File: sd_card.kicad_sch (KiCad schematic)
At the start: 19 parts, among them J1101 DM3AT-SF-PEJM5

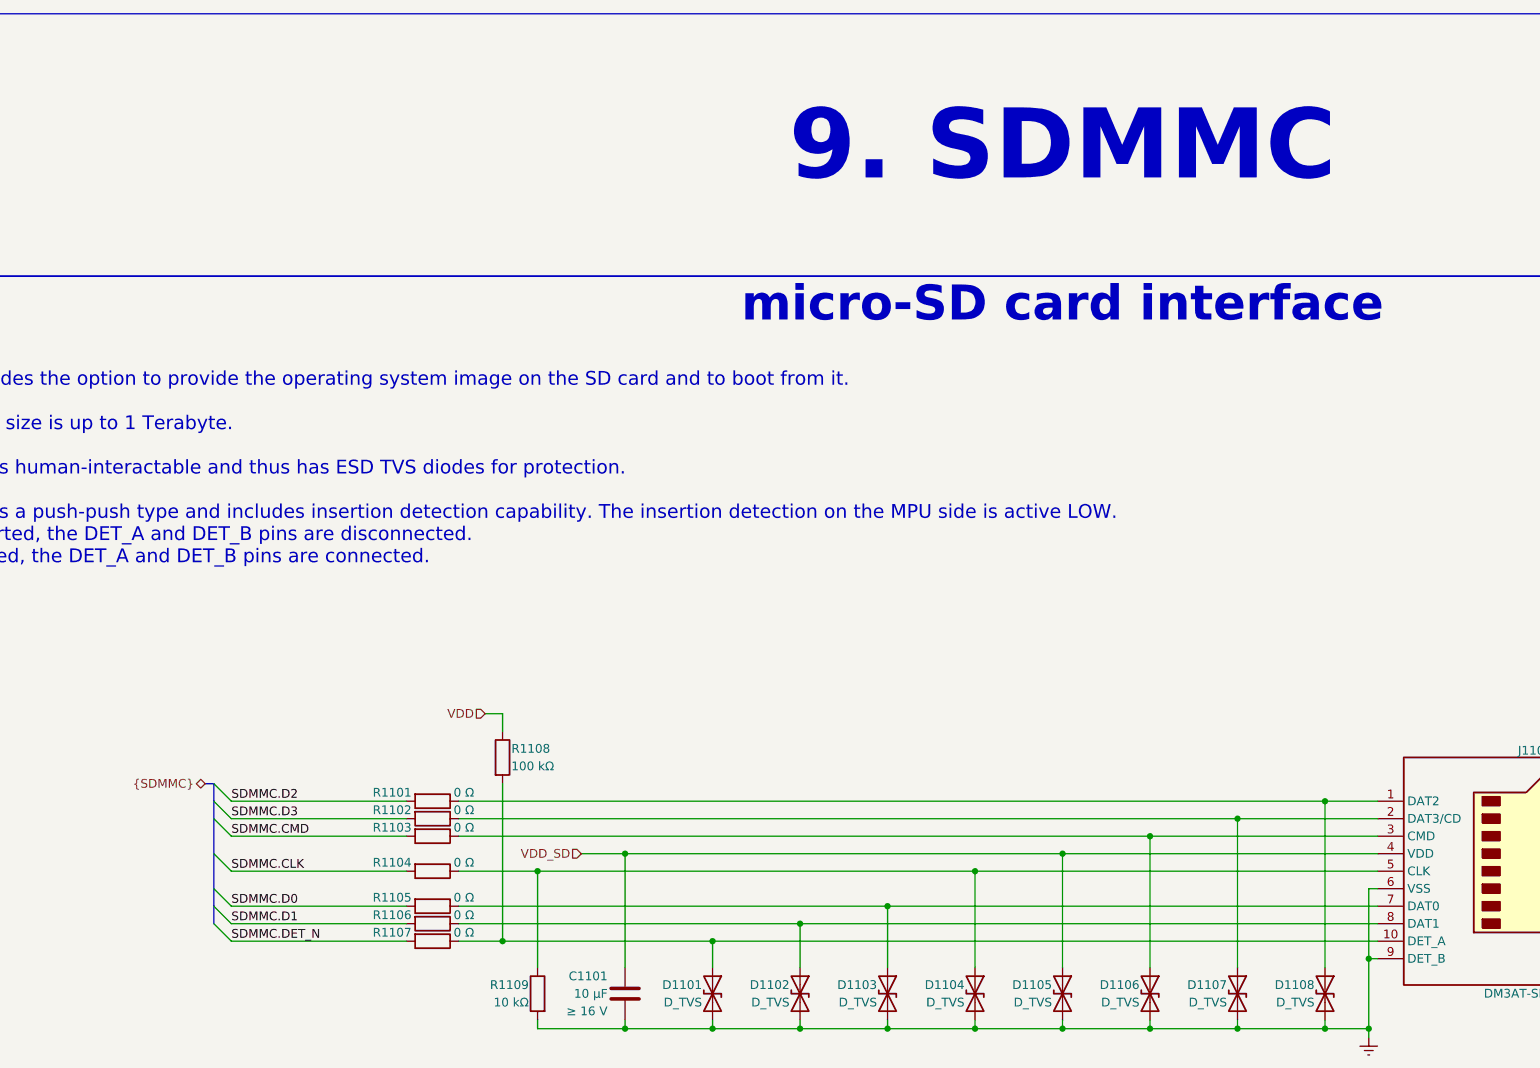
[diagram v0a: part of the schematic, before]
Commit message: Redo MPU pinout using STM32CubeMx
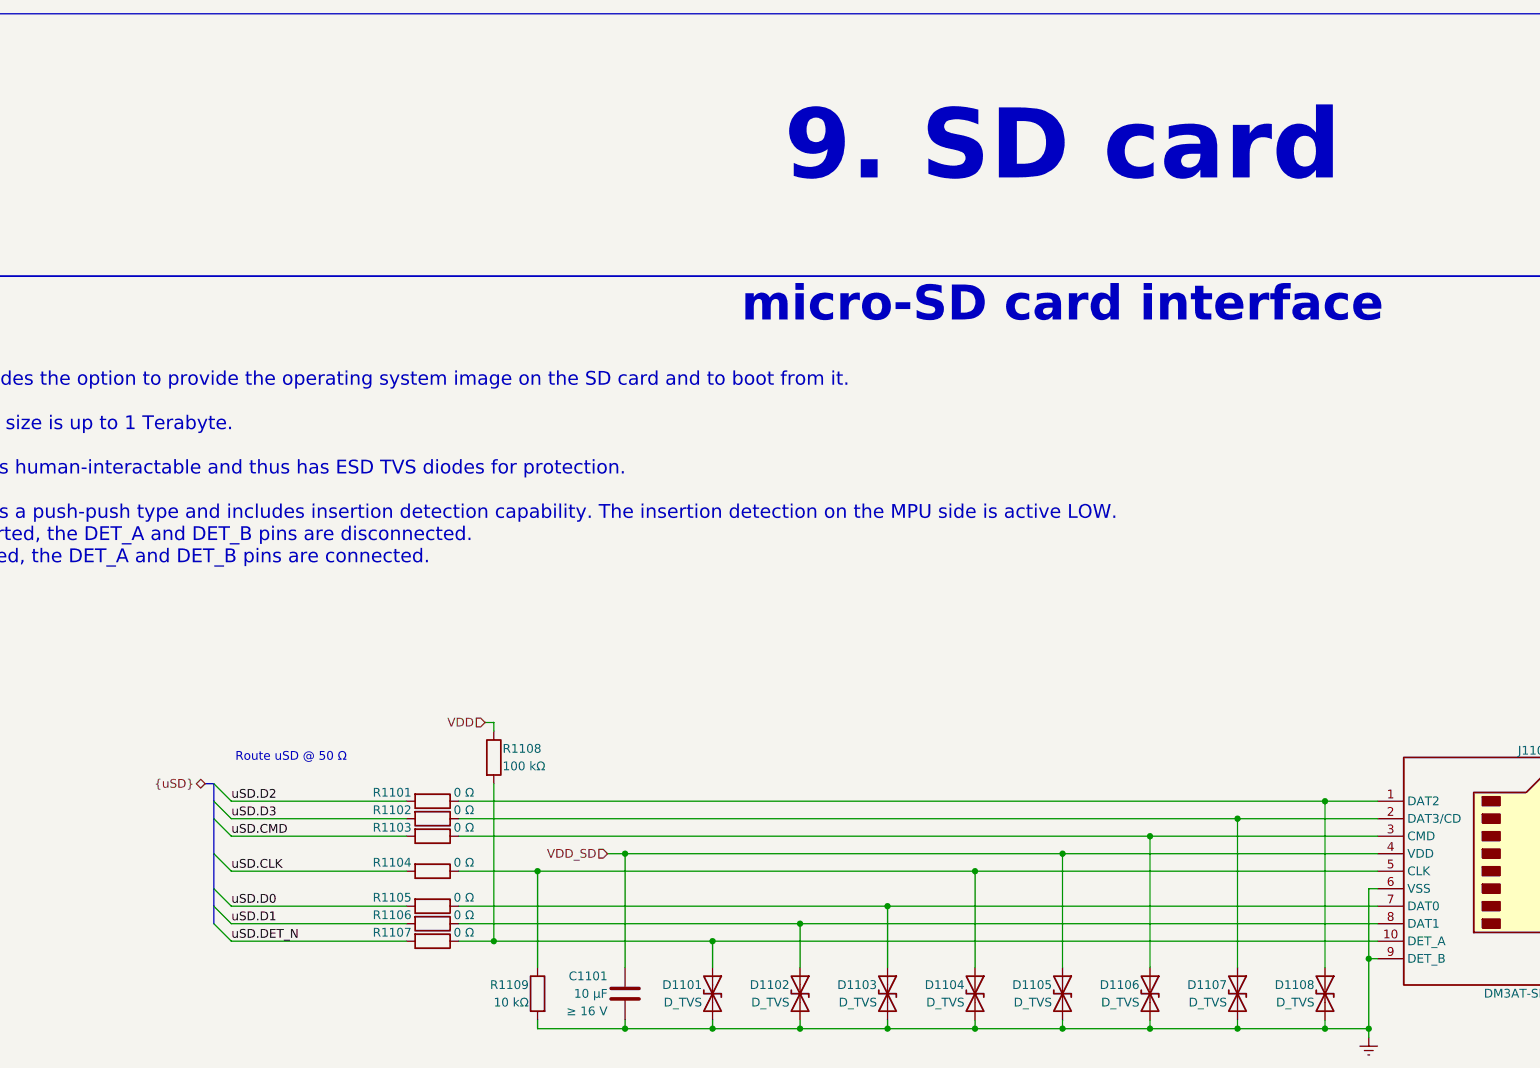
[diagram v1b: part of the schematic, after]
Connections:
- net SDMMC.CLK renamed uSD.CLK
- net SDMMC.CMD renamed uSD.CMD
- net SDMMC.D0 renamed uSD.D0
- net SDMMC.D1 renamed uSD.D1
- net SDMMC.D2 renamed uSD.D2
- net SDMMC.D3 renamed uSD.D3
- net SDMMC.DET_N renamed uSD.DET_N
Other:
- note added: "Route uSD @ 50 Ω"
- moved on the sheet: R1108
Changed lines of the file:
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@@
 		(rev "v0.0.1")
+	)
+	(text "Route uSD @ 50 Ω"
+		(exclude_from_sim no)
+		(at 105.664 120.65 0)
+		(effects
+			(font
+				(size 1.27 1.27)
+				(color 194 0 194 1)
+			)
+			(justify right)
+		)
 	)
 	(text_box "micro-SD card interface provides the option to provide the operating system image on the SD card and to boot from it.\n\nThe supported micro-SD card size is up to 1 Terabyte.\n\nThe micro-SD card interface is human-interactable and thus has ESD TVS diodes for protection.\n\nThe micro-SD card interface is a push-push type and includes insertion detection capability. The insertion detection on the MPU side is active LOW.\nWhen the SD card is not inserted, the DET_A and DET_B pins are disconnected.\nWhen the SD card is connected, the DET_A and DET_B pins are connected."
@@
 		)
 	)
-	(text_box "9. SDMMC"
+	(text_box "9. SD card"
 		(exclude_from_sim no)
 		(at 12.7 12.7 0)
@@
 	)
 	(junction
+		(at 127 147.32)
+		(diameter 0)
+		(color 0 0 0 0)
+	)
+	(junction
 		(at 158.75 160.02)
 		(diameter 0)
@@
 	)
 	(junction
-		(at 128.27 147.32)
-		(diameter 0)
-		(color 0 0 0 0)
-	)
-	(junction
 		(at 171.45 160.02)
 		(diameter 0)
@@
 	(wire
 		(pts
-			(xy 121.92 147.32) (xy 128.27 147.32)
+			(xy 121.92 147.32) (xy 127 147.32)
 		)
 		(stroke
@@
 	(wire
 		(pts
-			(xy 139.7 134.62) (xy 146.05 134.62)
+			(xy 143.51 134.62) (xy 146.05 134.62)
 		)
 		(stroke
@@
 	(wire
 		(pts
-			(xy 128.27 124.46) (xy 128.27 147.32)
+			(xy 127 124.46) (xy 127 147.32)
 		)
 		(stroke
@@
 	(wire
 		(pts
+			(xy 127 147.32) (xy 158.75 147.32)
+		)
+		(stroke
+			(width 0)
+			(type default)
+		)
+	)
+	(wire
+		(pts
 			(xy 146.05 158.75) (xy 146.05 160.02)
 		)
@@
 	(wire
 		(pts
-			(xy 125.73 114.3) (xy 128.27 114.3)
+			(xy 125.73 115.57) (xy 127 115.57)
 		)
 		(stroke
@@
 	(wire
 		(pts
-			(xy 128.27 147.32) (xy 158.75 147.32)
-		)
-		(stroke
-			(width 0)
-			(type default)
-		)
-	)
-	(wire
-		(pts
 			(xy 209.55 158.75) (xy 209.55 160.02)
 		)
@@
 	(wire
 		(pts
-			(xy 128.27 114.3) (xy 128.27 116.84)
+			(xy 127 115.57) (xy 127 116.84)
 		)
 		(stroke
@@
 		)
 	)
-	(label "SDMMC.DET_N"
+	(label "uSD.DET_N"
 		(at 88.9 147.32 0)
 		(effects
@@
 		)
 	)
-	(label "SDMMC.D3"
+	(label "uSD.D3"
 		(at 88.9 129.54 0)
 		(effects
@@
 		)
 	)
-	(label "SDMMC.D2"
+	(label "uSD.D2"
 		(at 88.9 127 0)
 		(effects
@@
 		)
 	)
-	(label "SDMMC.CMD"
+	(label "uSD.CMD"
 		(at 88.9 132.08 0)
 		(effects
@@
 		)
 	)
-	(label "SDMMC.D0"
+	(label "uSD.D0"
 		(at 88.9 142.24 0)
 		(effects
@@
 		)
 	)
-	(label "SDMMC.D1"
+	(label "uSD.D1"
 		(at 88.9 144.78 0)
 		(effects
@@
 		)
 	)
-	(label "SDMMC.CLK"
+	(label "uSD.CLK"
 		(at 88.9 137.16 0)
 		(effects
@@
 		)
 	)
-	(hierarchical_label "{SDMMC}"
+	(hierarchical_label "{uSD}"
 		(shape bidirectional)
 		(at 85.09 124.46 180)
@@
 	(hierarchical_label "VDD"
 		(shape input)
-		(at 125.73 114.3 180)
+		(at 125.73 115.57 180)
 		(effects
 			(font
@@
 	(hierarchical_label "VDD_SD"
 		(shape input)
-		(at 139.7 134.62 180)
+		(at 143.51 134.62 180)
 		(effects
 			(font
@@
 			)
 			(justify right)
+		)
+	)
+	(rule_area
+		(polyline
+			(pts
+				(xy 100.33 125.73) (xy 102.87 125.73) (xy 102.87 146.05) (xy 100.33 146.05)
+			)
+			(stroke
+				(width 0)
+				(type dash)
+			)
+			(fill
+				(type none)
+			)
+		)
+	)
+	(rule_area
+		(polyline
+			(pts
+				(xy 129.54 125.73) (xy 132.08 125.73) (xy 132.08 146.05) (xy 129.54 146.05)
+			)
+			(stroke
+				(width 0)
+				(type dash)
+			)
+			(fill
+				(type none)
+			)
+		)
+	)
+	(netclass_flag ""
+		(length 2.54)
+		(shape round)
+		(at 132.08 125.73 270)
+		(effects
+			(font
+				(size 1.27 1.27)
+			)
+			(justify right bottom)
+		)
+		(property "Netclass" "uSD"
+			(at 135.382 125.73 0)
+			(effects
+				(font
+					(size 1.27 1.27)
+				)
+				(justify left)
+			)
+		)
+		(property "Component Class" ""
+			(at -27.94 8.89 0)
+			(effects
+				(font
+					(size 1.27 1.27)
+					(italic yes)
+				)
+			)
+		)
+	)
+	(netclass_flag ""
+		(length 2.54)
+		(shape round)
+		(at 101.6 125.73 0)
+		(fields_autoplaced yes)
+		(effects
+			(font
+				(size 1.27 1.27)
+			)
+			(justify left bottom)
+		)
+		(property "Netclass" "uSD"
+			(at 102.2985 123.19 0)
+			(effects
+				(font
+					(size 1.27 1.27)
+				)
+				(justify left)
+			)
+		)
+		(property "Component Class" ""
+			(at -58.42 8.89 0)
+			(effects
+				(font
+					(size 1.27 1.27)
+					(italic yes)
+				)
+			)
 		)
 	)
@@
 	(symbol
 		(lib_id "Device:R")
-		(at 128.27 120.65 0)
+		(at 127 120.65 0)
 		(unit 1)
 		(exclude_from_sim no)
@@
 		(dnp no)
 		(property "Reference" "R1108"
-			(at 129.54 119.38 0)
+			(at 128.27 119.38 0)
 			(effects
 				(font
@@
 		)
 		(property "Value" "100 kΩ"
-			(at 129.54 121.92 0)
+			(at 128.27 121.92 0)
 			(effects
 				(font
@@
 		)
 		(property "Footprint" "perfect_footprints:R_0402_1005Metric"
-			(at 126.492 120.65 90)
+			(at 125.222 120.65 90)
 			(effects
 				(font
@@
 		)
 		(property "Datasheet" "https://www.we-online.com/components/products/datasheet/560112110019.pdf"
-			(at 128.27 120.65 0)
+			(at 127 120.65 0)
 			(effects
 				(font
@@
 		)
 		(property "Description" "Resistor"
-			(at 128.27 120.65 0)
+			(at 127 120.65 0)
 			(effects
 				(font
@@
 		)
 		(property "MPN" "560112110019"
-			(at 128.27 120.65 0)
+			(at 127 120.65 0)
 			(effects
 				(font
@@
 		)
 		(property "Manufacturer" "Würth Elektronik"
-			(at 128.27 120.65 0)
-			(effects
-				(font
+			(at 127 120.65 0)
+			(effects
+				(font

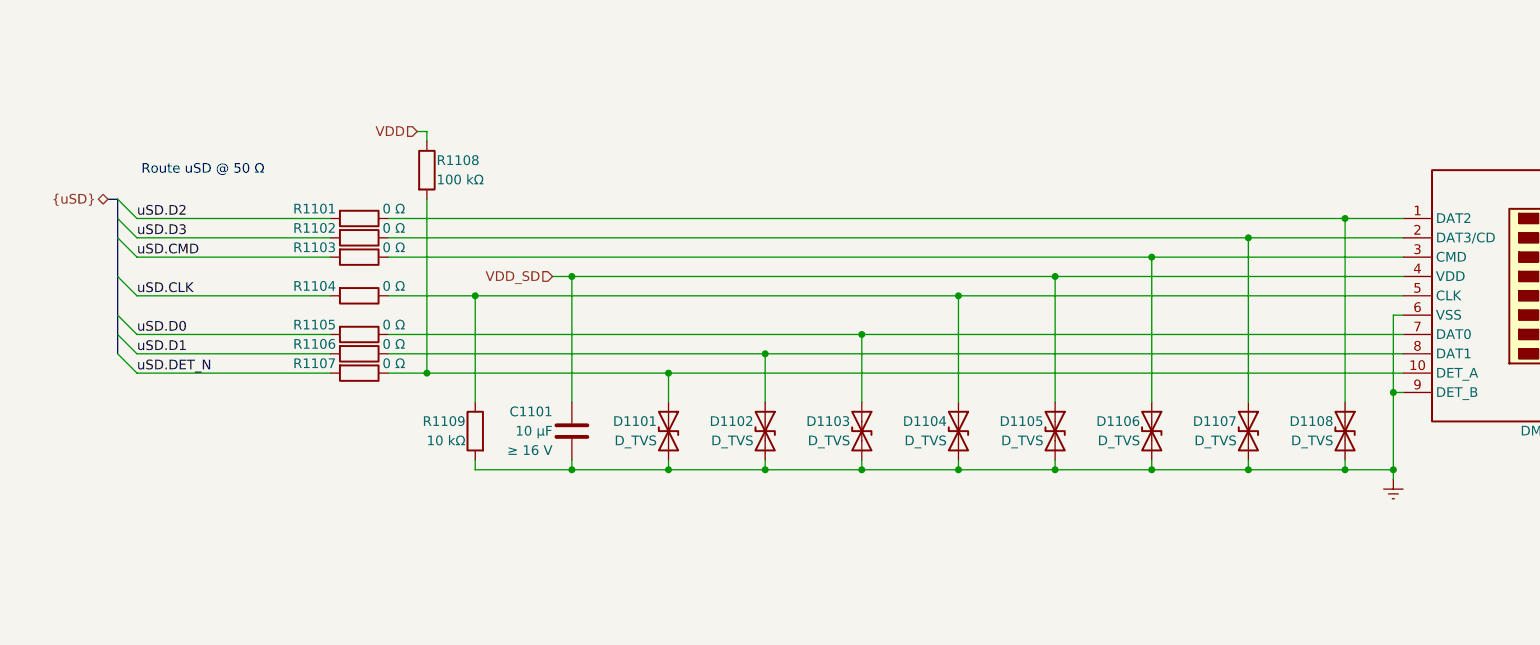
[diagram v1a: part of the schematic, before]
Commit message: Add additional info to passives
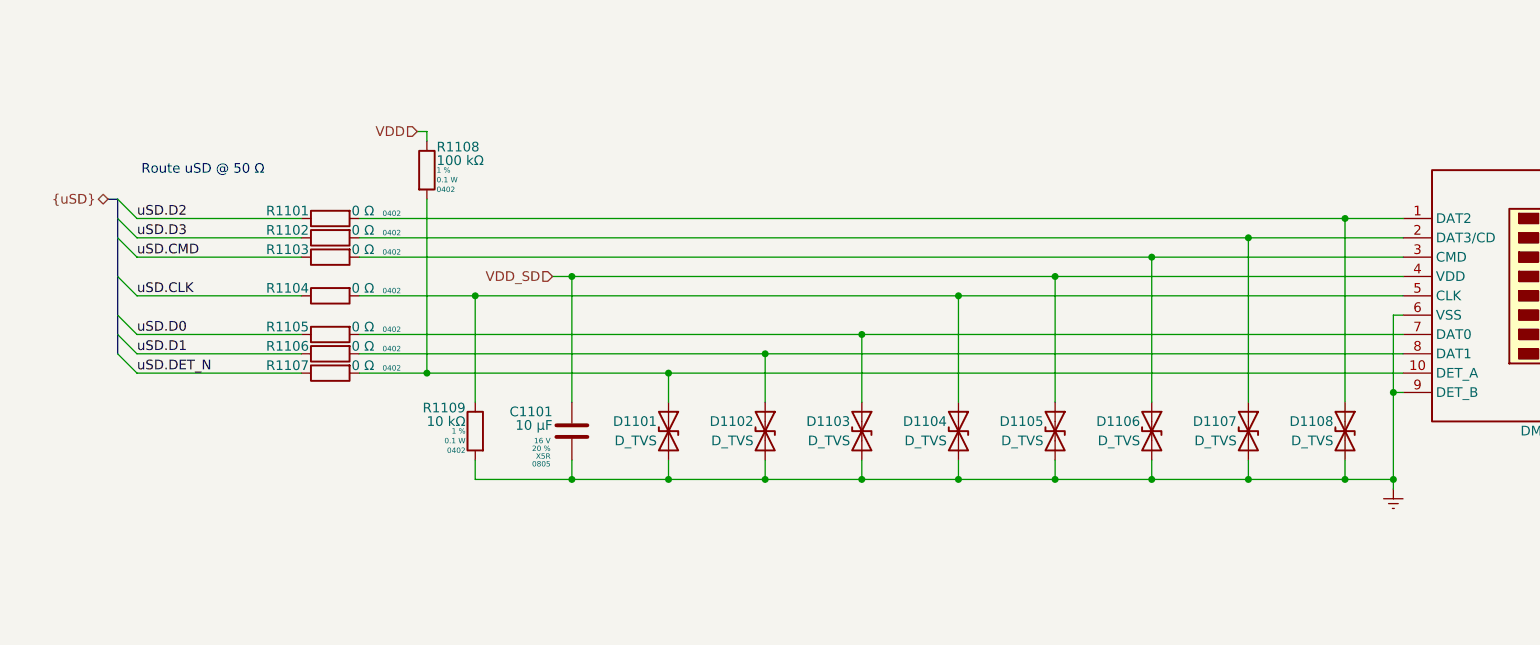
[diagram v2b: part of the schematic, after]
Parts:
- C1101: Size (none) -> 0805; Temperature coefficient (none) -> X5R; Tolerance (none) -> 20 %; Voltage rating ≥ 16 V -> 16 V
- R1101, R1102, R1103, R1104, R1105, R1106, R1107: footprint perfect_footprints:R_0402_1005Metric -> (none); MPN 560112110020 -> (none); Manufacturer Würth Elektronik -> (none); Size (none) -> 0402
- R1108: MPN 560112110019 -> (none); Manufacturer Würth Elektronik -> (none); Power rating (none) -> 0.1 W; Size (none) -> 0402; Tolerance (none) -> 1 %
- R1109: MPN 560112110020 -> (none); Manufacturer Würth Elektronik -> (none); Power rating (none) -> 0.1 W; Size (none) -> 0402; Tolerance (none) -> 1 %
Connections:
- net uSD.CLK: now also R1104.1; no longer R1104.2
- net uSD.CMD: now also R1103.1; no longer R1103.2
- net uSD.D0: now also R1105.1; no longer R1105.2
- net uSD.D1: now also R1106.1; no longer R1106.2
- net uSD.D2: now also R1101.1; no longer R1101.2
- net uSD.D3: now also R1102.1; no longer R1102.2
- net uSD.DET_N: now also R1107.1; no longer R1107.2
- net at D1102.1 (A1), J1101.8 (DAT1): now also R1106.2; no longer R1106.1
- net at D1108.1 (A1), J1101.1 (DAT2): now also R1101.2; no longer R1101.1
- net at D1103.1 (A1), J1101.7 (DAT0): now also R1105.2; no longer R1105.1
- net at D1107.1 (A1), J1101.2 (DAT3/CD): now also R1102.2; no longer R1102.1
- net at D1101.1 (A1), J1101.10 (DET_A), R1108.2: now also R1107.2; no longer R1107.1
- net at D1106.1 (A1), J1101.3 (CMD): now also R1103.2; no longer R1103.1
- net at D1104.1 (A1), J1101.5 (CLK), R1109.1: now also R1104.2; no longer R1104.1

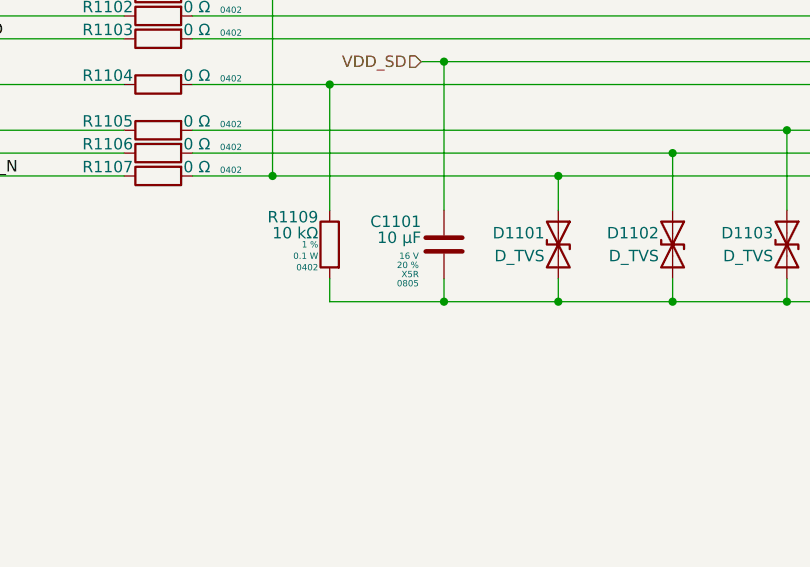
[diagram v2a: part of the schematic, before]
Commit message: Update capacitor BOM
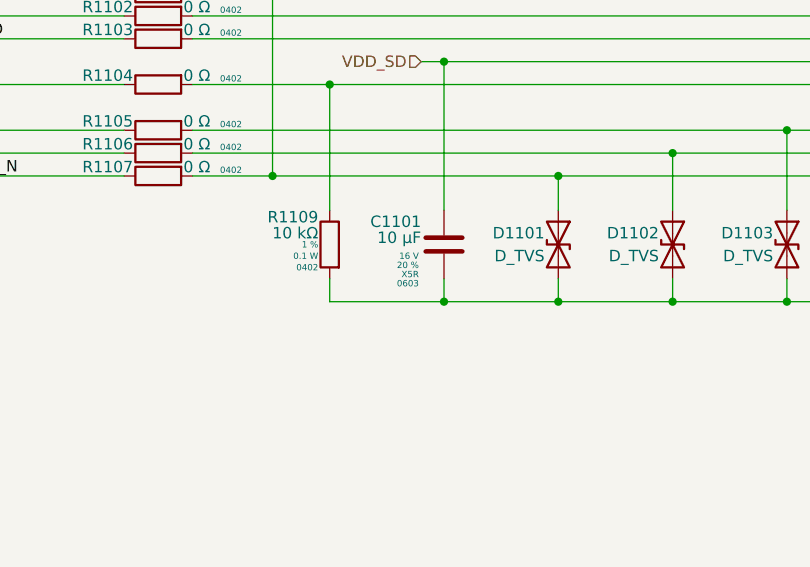
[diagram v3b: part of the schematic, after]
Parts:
- C1101: footprint (none) -> Capacitor_SMD:C_0603_1608Metric; Digi-Key Part Number (none) -> 490-13248-1-ND; MPN (none) -> GRM188R6YA106MA73D; Manufacturer (none) -> Murata Electronics; Size 0805 -> 0603
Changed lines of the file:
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@@
 			)
 		)
-		(property "Footprint" ""
+		(property "Footprint" "Capacitor_SMD:C_0603_1608Metric"
 			(at 145.0848 158.75 0)
 			(effects
@@
 			)
 		)
-		(property "Datasheet" ""
+		(property "Datasheet" "https://search.murata.co.jp/Ceramy/image/img/A01X/G101/ENG/GRM188R6YA106MA73-01A.pdf"
 			(at 146.05 154.94 0)
 			(effects
@@
 			)
 		)
-		(property "Description" ""
+		(property "Description" "10 µF ±20% 35V Ceramic Capacitor X5R 0603 (1608 Metric)"
 			(at 146.05 154.94 0)
 			(effects
@@
 			)
 		)
-		(property "MPN" ""
+		(property "MPN" "GRM188R6YA106MA73D"
 			(at 146.05 154.94 0)
 			(effects
@@
 			)
 		)
-		(property "Manufacturer" ""
+		(property "Manufacturer" "Murata Electronics"
 			(at 146.05 154.94 0)
 			(effects
@@
 			)
 		)
-		(property "Size" "0805"
+		(property "Size" "0603"
 			(at 143.256 159.258 0)
 			(effects
@@
 			)
 		)
+		(property "Digi-Key Part Number" "490-13248-1-ND"
+			(at 146.05 154.94 0)
+			(effects
+				(font
+					(size 1.27 1.27)
+				)
+				(hide yes)
+			)
+		)
